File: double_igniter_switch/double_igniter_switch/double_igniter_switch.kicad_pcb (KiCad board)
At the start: 2 copper layers, 45 x 27 mm, 16 parts, among them J1 Speaker_terminal, J2 Conn_02x04_Odd_Even, Q1 IPD50N06S4L-12, Q2 IPD50N06S4L-12, U1 MCP1416, U2 MCP1416

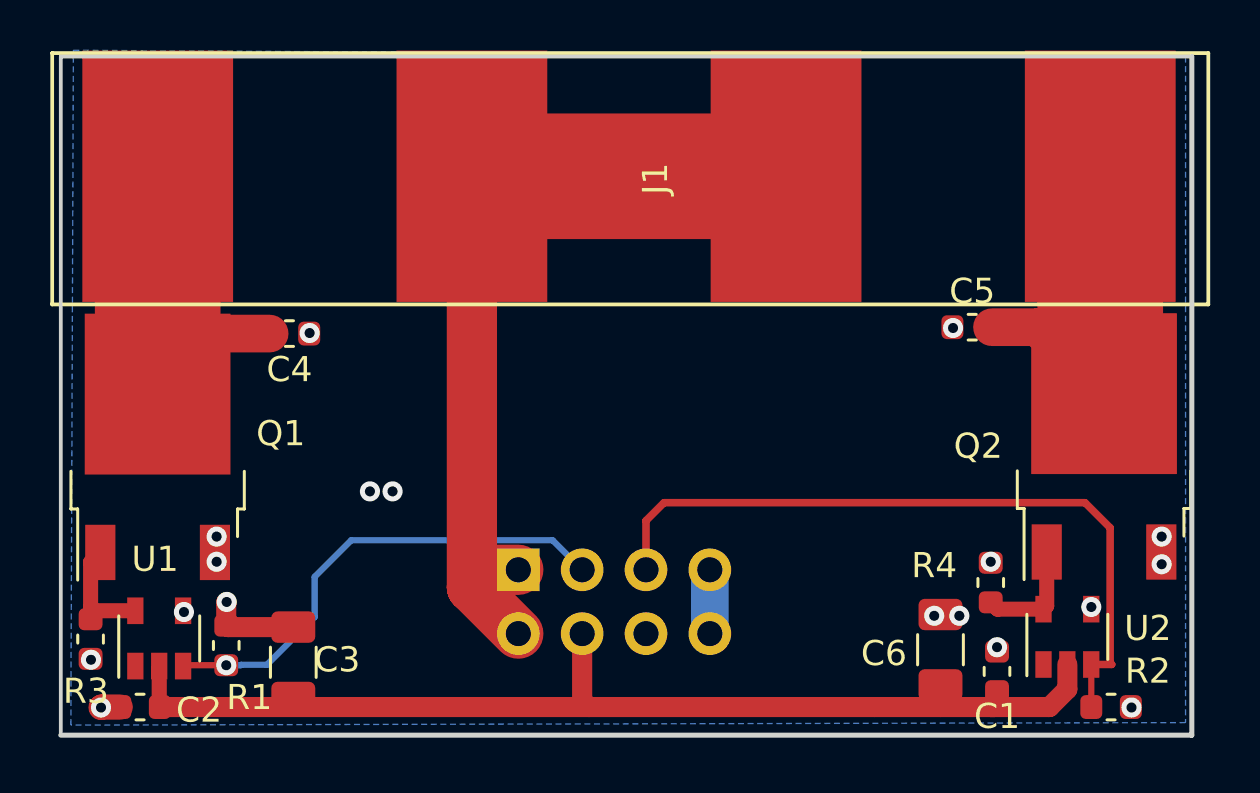
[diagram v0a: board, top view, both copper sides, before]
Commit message: added esd diode and free wheeling dioed to mosfet module, removed gate drive, changed pinout
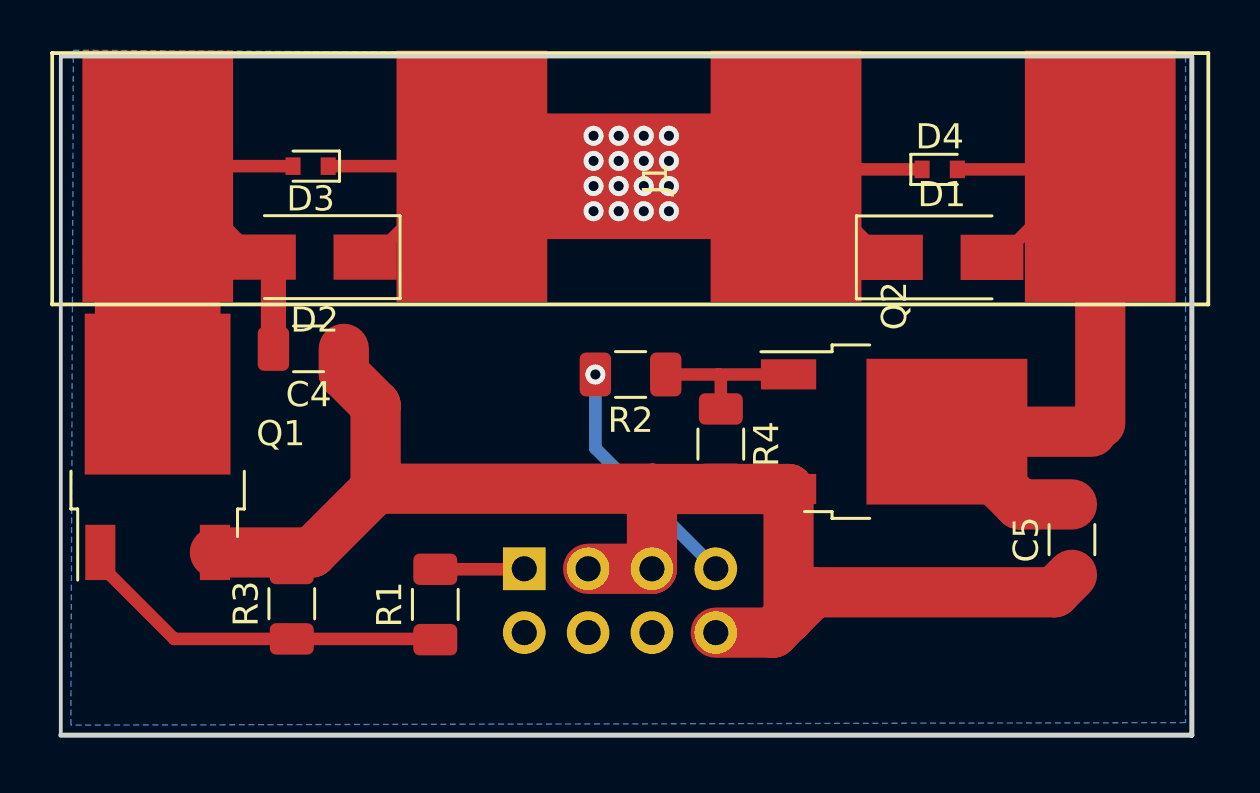
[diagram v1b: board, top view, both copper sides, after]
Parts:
- removed C1, C2: 100n, Capacitor_SMD:C_0603_1608Metric
- removed C3, C6: 10µ 50V, Capacitor_SMD:C_1206_3216Metric
- removed U1, U2: MCP1416, Package_TO_SOT_SMD:SOT-23-5
- added D1: MBRA340, Diode_SMD:D_SMA, F.Cu at (117.0, 46.0)
- added D2: MBRA340, Diode_SMD:D_SMA, F.Cu at (92.1, 46.0)
- added D3: VESD33C1-02V, Diode_SMD:D_SOD-523, F.Cu at (91.9, 42.4)
- added D4: VESD33C1-02V, Diode_SMD:D_SOD-523, F.Cu at (117.0, 42.5)
- C4, C5: footprint Capacitor_SMD:C_0603_1608Metric -> Resistor_SMD:R_1206_3216Metric
- R1, R2, R3, R4: footprint Resistor_SMD:R_0603_1608Metric -> Resistor_SMD:R_1206_3216Metric
- moved R2 23.2 mm to (104.7, 50.6), turned to 180 degrees
- moved R4 12.1 mm to (108.3, 53.4), turned to 270 degrees
- moved C5 9.34 mm to (122.2, 57.2), turned to 90 degrees
- moved R1 8.48 mm to (96.9, 59.8)
- moved Q2 8.37 mm to (115.2, 52.9), turned to 0 degrees
- moved R3 8.13 mm to (91.2, 59.8), turned to 90 degrees
- moved C4 0.98 mm to (91.9, 49.6)
- moved J2 0.24 mm to (100.4, 58.4)
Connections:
- J2 pad 1: VCC -> /SW_Ch1
- J2 pad 3: /SW_Ch1 -> GND
- J2 pad 4: +10V -> VCC
- J2 pad 5: /SW_Ch2 -> GND
- J2 pad 6: (no net) -> VCC
- J2 pad 7: GND -> /SW_Ch2
- R1 pad 1: /SW_Ch1 -> Net-(Q1-Pad1)
- R1 pad 2: GND -> /SW_Ch1
- R2 pad 1: /SW_Ch2 -> Net-(Q2-Pad1)
- R2 pad 2: GND -> /SW_Ch2
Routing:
- net GND: track 6.95 -> 56.0 mm, vias 18 -> 0
- net +10V: track 43.7 -> 0.00 mm
- net /SW_Ch2: track 29.1 -> 9.71 mm, vias 0 -> 1
- net /Ch2: track 14.3 -> 33.2 mm
- net /SW_Ch1: track 19.4 -> 3.55 mm, vias 1 -> 0
- net Net-(Q1-Pad1): track 4.64 -> 15.1 mm
- net /Ch1: track 14.1 -> 23.6 mm
- net Net-(Q2-Pad1): track 4.54 -> 6.29 mm
- net VCC: track 33.6 -> 35.0 mm, vias 0 -> 16
- added copper zone on B.Cu, net VCC
- removed copper zone on B.Cu, net GND
